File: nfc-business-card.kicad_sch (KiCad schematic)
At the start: 8 parts, among them U1 NT3H2111W0FHKH

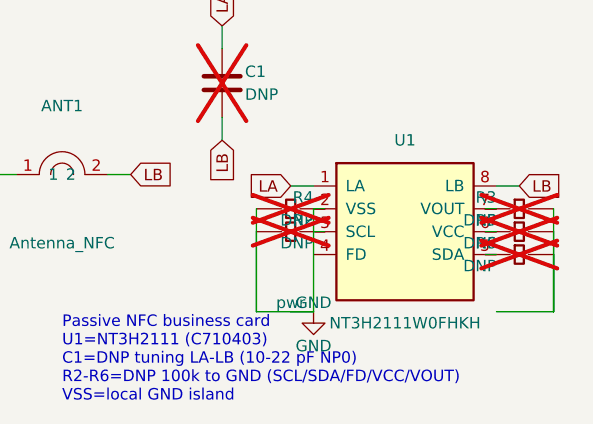
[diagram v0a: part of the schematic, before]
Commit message: fix: route LB under LA skirt without shorting VOUT
Keep the westbound VOUT crossing on F.Cu above the LA skirt, and drop
to B.Cu only in the clearance column between VCC and VOUT. Lower the
KiCad min track width to the JLC floor so intentional 0.15 mm NC stubs
pass DRC.
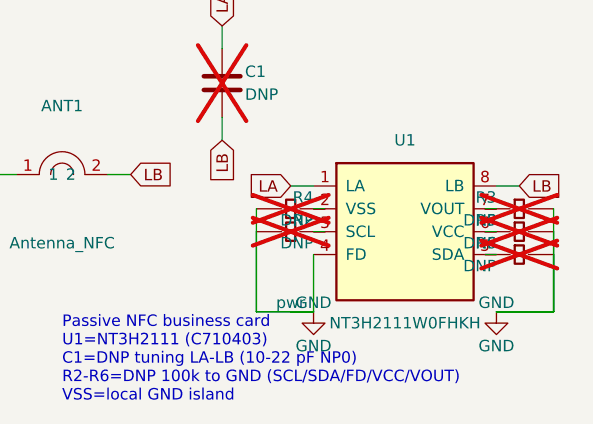
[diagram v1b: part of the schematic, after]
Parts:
- R2, R3, R4, R5, R6: LCSC Part # C25744 -> C60491
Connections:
- net GND: now also R3.1, R5.1, R6.1, U1.4 (FD); no longer R4.2, U1.2 (VSS)
- new net: R4.2, U1.2 (VSS)
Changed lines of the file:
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@@
+	)
+	(symbol
+		(lib_id "NFC_BusinessCard:GND")
+		(at 137.16 93.98 0)
+		(unit 1)
+		(exclude_from_sim no)
+		(in_bom no)
+		(on_board no)
+		(dnp no)
+		(property "Reference" "#PWR02" (at 137.16 100.33 0) (effects (font (size 1.27 1.27)) (hide yes)))
+		(property "Value" "GND" (at 137.16 97.79 0) (effects (font (size 1.27 1.27))))
+		(property "Footprint" "" (at 137.16 93.98 0) (effects (font (size 1.27 1.27)) (hide yes)))
+		(pin "1")
+		(instances (project "nfc-business-card" (path "/db0e1d12-1252-490b-9c29-4e9a9001ab69" (reference "#PWR02") (unit 1))))
 	)
 	(symbol
@@
 	(wire (pts (xy 106.68 64.77) (xy 106.68 62.23)) (stroke (width 0) (type default)))
 	(global_label "LA" (shape input) (at 106.68 62.23 90) (effects (font (size 1.27 1.27)) (justify left bottom)))
-	(wire (pts (xy 116.84 82.55) (xy 116.84 93.98)) (stroke (width 0) (type default)))
+	(wire (pts (xy 116.84 87.63) (xy 116.84 93.98)) (stroke (width 0) (type default)))
 	(wire (pts (xy 116.84 93.98) (xy 114.3 93.98)) (stroke (width 0) (type default)))
 	(symbol
@@
 		(property "Value" "DNP" (at 116.84 86.36 90) (effects (font (size 1.27 1.27)) (justify left)))
 		(property "Footprint" "NFC_BusinessCard:R_0402_1005Metric" (at 114.3 85.09 90) (effects (font (size 1.27 1.27)) (hide yes)))
-		(property "LCSC Part #" "C25744" (at 114.3 85.09 90) (effects (font (size 1.27 1.27)) (hide yes)))
+		(property "LCSC Part #" "C60491" (at 114.3 85.09 90) (effects (font (size 1.27 1.27)) (hide yes)))
 		(pin "1")
 		(pin "2")
@@
 	(wire (pts (xy 116.84 85.09) (xy 118.11 85.09)) (stroke (width 0) (type default)))
 	(wire (pts (xy 110.49 85.09) (xy 110.49 93.98)) (stroke (width 0) (type default)))
+	(wire (pts (xy 110.49 93.98) (xy 116.84 93.98)) (stroke (width 0) (type default)))
 	(symbol
 		(lib_id "NFC_BusinessCard:R_0402")
@@
 		(property "Value" "DNP" (at 116.84 83.82 90) (effects (font (size 1.27 1.27)) (justify left)))
 		(property "Footprint" "NFC_BusinessCard:R_0402_1005Metric" (at 114.3 82.55 90) (effects (font (size 1.27 1.27)) (hide yes)))
-		(property "LCSC Part #" "C25744" (at 114.3 82.55 90) (effects (font (size 1.27 1.27)) (hide yes)))
+		(property "LCSC Part #" "C60491" (at 114.3 82.55 90) (effects (font (size 1.27 1.27)) (hide yes)))
 		(pin "1")
 		(pin "2")
@@
 	(wire (pts (xy 116.84 82.55) (xy 118.11 82.55)) (stroke (width 0) (type default)))
 	(wire (pts (xy 110.49 82.55) (xy 110.49 93.98)) (stroke (width 0) (type default)))
+	(wire (pts (xy 110.49 93.98) (xy 116.84 93.98)) (stroke (width 0) (type default)))
 	(symbol
 		(lib_id "NFC_BusinessCard:R_0402")
@@
 		(property "Value" "DNP" (at 137.16 83.82 270) (effects (font (size 1.27 1.27)) (justify left)))
 		(property "Footprint" "NFC_BusinessCard:R_0402_1005Metric" (at 139.7 82.55 270) (effects (font (size 1.27 1.27)) (hide yes)))
-		(property "LCSC Part #" "C25744" (at 139.7 82.55 270) (effects (font (size 1.27 1.27)) (hide yes)))
+		(property "LCSC Part #" "C60491" (at 139.7 82.55 270) (effects (font (size 1.27 1.27)) (hide yes)))
 		(pin "1")
 		(pin "2")
@@
 	(wire (pts (xy 137.16 82.55) (xy 135.89 82.55)) (stroke (width 0) (type default)))
 	(wire (pts (xy 143.51 82.55) (xy 143.51 93.98)) (stroke (width 0) (type default)))
+	(wire (pts (xy 143.51 93.98) (xy 137.16 93.98)) (stroke (width 0) (type default)))
 	(symbol
 		(lib_id "NFC_BusinessCard:R_0402")
@@
 		(property "Value" "DNP" (at 137.16 86.36 270) (effects (font (size 1.27 1.27)) (justify left)))
 		(property "Footprint" "NFC_BusinessCard:R_0402_1005Metric" (at 139.7 85.09 270) (effects (font (size 1.27 1.27)) (hide yes)))
-		(property "LCSC Part #" "C25744" (at 139.7 85.09 270) (effects (font (size 1.27 1.27)) (hide yes)))
+		(property "LCSC Part #" "C60491" (at 139.7 85.09 270) (effects (font (size 1.27 1.27)) (hide yes)))
 		(pin "1")
 		(pin "2")
@@
 	(wire (pts (xy 137.16 85.09) (xy 135.89 85.09)) (stroke (width 0) (type default)))
 	(wire (pts (xy 143.51 85.09) (xy 143.51 93.98)) (stroke (width 0) (type default)))
+	(wire (pts (xy 143.51 93.98) (xy 137.16 93.98)) (stroke (width 0) (type default)))
 	(symbol
 		(lib_id "NFC_BusinessCard:R_0402")
-		(at 139.7 87.63 270)
+		(at 139.7 87.63000000000001 270)
 		(unit 1)
 		(exclude_from_sim no)
@@
 		(on_board yes)
 		(dnp yes)
-		(property "Reference" "R6" (at 137.16 86.36 270) (effects (font (size 1.27 1.27)) (justify left)))
-		(property "Value" "DNP" (at 137.16 88.89999999999999 270) (effects (font (size 1.27 1.27)) (justify left)))
-		(property "Footprint" "NFC_BusinessCard:R_0402_1005Metric" (at 139.7 87.63 270) (effects (font (size 1.27 1.27)) (hide yes)))
-		(property "LCSC Part #" "C25744" (at 139.7 87.63 270) (effects (font (size 1.27 1.27)) (hide yes)))
+		(property "Reference" "R6" (at 137.16 86.36000000000001 270) (effects (font (size 1.27 1.27)) (justify left)))
+		(property "Value" "DNP" (at 137.16 88.9 270) (effects (font (size 1.27 1.27)) (justify left)))
+		(property "Footprint" "NFC_BusinessCard:R_0402_1005Metric" (at 139.7 87.63000000000001 270) (effects (font (size 1.27 1.27)) (hide yes)))
+		(property "LCSC Part #" "C60491" (at 139.7 87.63000000000001 270) (effects (font (size 1.27 1.27)) (hide yes)))
 		(pin "1")
 		(pin "2")
 		(instances (project "nfc-business-card" (path "/db0e1d12-1252-490b-9c29-4e9a9001ab69" (reference "R6") (unit 1))))
 	)
-	(wire (pts (xy 137.16 87.63) (xy 135.89 87.63)) (stroke (width 0) (type default)))
-	(wire (pts (xy 143.51 87.63) (xy 143.51 93.98)) (stroke (width 0) (type default)))
-	(wire (pts (xy 110.49 93.98) (xy 116.84 93.98)) (stroke (width 0) (type default)))
-	(wire (pts (xy 116.84 93.98) (xy 116.84 93.98)) (stroke (width 0) (type default)))
+	(wire (pts (xy 137.16 87.63000000000001) (xy 135.89 87.63000000000001)) (stroke (width 0) (type default)))
+	(wire (pts (xy 143.51 87.63000000000001) (xy 143.51 93.98)) (stroke (width 0) (type default)))
 	(wire (pts (xy 143.51 93.98) (xy 137.16 93.98)) (stroke (width 0) (type default)))
-	(wire (pts (xy 137.16 93.98) (xy 137.16 93.98)) (stroke (width 0) (type default)))
 	(text "Passive NFC business card\nU1=NT3H2111 (C710403)\nC1=DNP tuning LA-LB (10-22 pF NP0)\nR2-R6=DNP 100k to GND (SCL/SDA/FD/VCC/VOUT)\nVSS=local GND island"
 		(at 88.9 104.14 0)

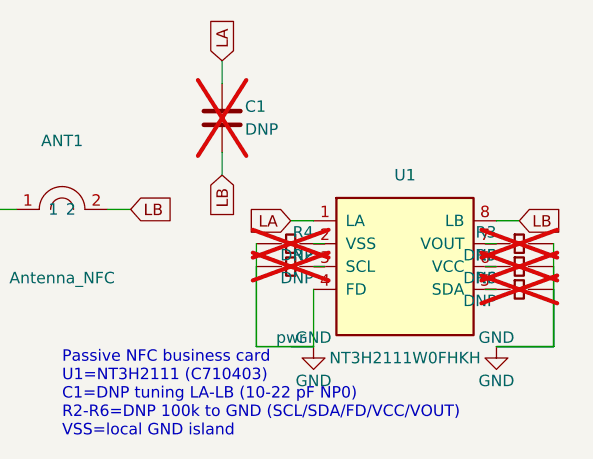
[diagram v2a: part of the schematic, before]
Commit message: fix: clear schematic parity and stop greenwashing DRC warnings
Correct eeschema Y mapping for U1–R NC wiring, skip degenerate VOUT
segments, require CLI checks to fail on unaccepted warnings/parity, and
only allowlist LA/LB for clearance (not crossings).
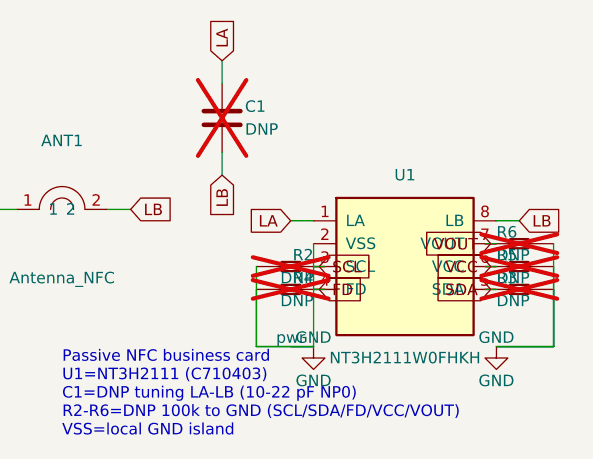
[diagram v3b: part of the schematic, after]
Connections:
- net GND: now also R2.2, R3.2, R4.2, R5.2, R6.2, U1.2 (VSS); no longer R2.1, R3.1, R4.1, R5.1, R6.1, U1.4 (FD)
- net VCC: now reaches U1.6 (VCC)
- net VCC: now also R5.1; no longer R5.2
- net VOUT: now reaches U1.7 (VOUT)
- net VOUT: now also R6.1; no longer R3.2
- net SDA: now reaches U1.5 (SDA)
- net SDA: now also R3.1; no longer R6.2
- net SCL: now reaches U1.3 (SCL)
- net SCL: now also R2.1; no longer R2.2
- new net FD: R4.1, U1.4 (FD)
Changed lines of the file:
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@@
 	(wire (pts (xy 106.68 64.77) (xy 106.68 62.23)) (stroke (width 0) (type default)))
 	(global_label "LA" (shape input) (at 106.68 62.23 90) (effects (font (size 1.27 1.27)) (justify left bottom)))
-	(wire (pts (xy 116.84 87.63) (xy 116.84 93.98)) (stroke (width 0) (type default)))
+	(wire (pts (xy 116.84 82.55) (xy 116.84 93.98)) (stroke (width 0) (type default)))
 	(wire (pts (xy 116.84 93.98) (xy 114.3 93.98)) (stroke (width 0) (type default)))
 	(symbol
 		(lib_id "NFC_BusinessCard:R_0402")
-		(at 114.3 85.09 90)
+		(at 114.3 85.09 180)
 		(unit 1)
 		(exclude_from_sim no)
@@
 		(on_board yes)
 		(dnp yes)
-		(property "Reference" "R2" (at 116.84 83.82000000000001 90) (effects (font (size 1.27 1.27)) (justify left)))
-		(property "Value" "DNP" (at 116.84 86.36 90) (effects (font (size 1.27 1.27)) (justify left)))
-		(property "Footprint" "NFC_BusinessCard:R_0402_1005Metric" (at 114.3 85.09 90) (effects (font (size 1.27 1.27)) (hide yes)))
-		(property "LCSC Part #" "C60491" (at 114.3 85.09 90) (effects (font (size 1.27 1.27)) (hide yes)))
+		(property "Reference" "R2" (at 116.84 83.82000000000001 0) (effects (font (size 1.27 1.27)) (justify left)))
+		(property "Value" "DNP" (at 116.84 86.36 0) (effects (font (size 1.27 1.27)) (justify left)))
+		(property "Footprint" "NFC_BusinessCard:R_0402_1005Metric" (at 114.3 85.09 180) (effects (font (size 1.27 1.27)) (hide yes)))
+		(property "Description" "100k NC pull-down" (at 114.3 85.09 180) (effects (font (size 1.27 1.27)) (hide yes)))
+		(property "LCSC Part #" "C60491" (at 114.3 85.09 180) (effects (font (size 1.27 1.27)) (hide yes)))
 		(pin "1")
 		(pin "2")
@@
 	)
 	(wire (pts (xy 116.84 85.09) (xy 118.11 85.09)) (stroke (width 0) (type default)))
+	(global_label "SCL" (shape input) (at 117.475 85.09 0) (effects (font (size 1.27 1.27)) (justify left bottom)))
 	(wire (pts (xy 110.49 85.09) (xy 110.49 93.98)) (stroke (width 0) (type default)))
 	(wire (pts (xy 110.49 93.98) (xy 116.84 93.98)) (stroke (width 0) (type default)))
 	(symbol
 		(lib_id "NFC_BusinessCard:R_0402")
-		(at 114.3 82.55 90)
+		(at 114.3 87.63000000000001 180)
 		(unit 1)
 		(exclude_from_sim no)
@@
 		(on_board yes)
 		(dnp yes)
-		(property "Reference" "R4" (at 116.84 81.28 90) (effects (font (size 1.27 1.27)) (justify left)))
-		(property "Value" "DNP" (at 116.84 83.82 90) (effects (font (size 1.27 1.27)) (justify left)))
-		(property "Footprint" "NFC_BusinessCard:R_0402_1005Metric" (at 114.3 82.55 90) (effects (font (size 1.27 1.27)) (hide yes)))
-		(property "LCSC Part #" "C60491" (at 114.3 82.55 90) (effects (font (size 1.27 1.27)) (hide yes)))
+		(property "Reference" "R4" (at 116.84 86.36000000000001 0) (effects (font (size 1.27 1.27)) (justify left)))
+		(property "Value" "DNP" (at 116.84 88.9 0) (effects (font (size 1.27 1.27)) (justify left)))
+		(property "Footprint" "NFC_BusinessCard:R_0402_1005Metric" (at 114.3 87.63000000000001 180) (effects (font (size 1.27 1.27)) (hide yes)))
+		(property "Description" "100k NC pull-down" (at 114.3 87.63000000000001 180) (effects (font (size 1.27 1.27)) (hide yes)))
+		(property "LCSC Part #" "C60491" (at 114.3 87.63000000000001 180) (effects (font (size 1.27 1.27)) (hide yes)))
 		(pin "1")
 		(pin "2")
 		(instances (project "nfc-business-card" (path "/db0e1d12-1252-490b-9c29-4e9a9001ab69" (reference "R4") (unit 1))))
 	)
-	(wire (pts (xy 116.84 82.55) (xy 118.11 82.55)) (stroke (width 0) (type default)))
-	(wire (pts (xy 110.49 82.55) (xy 110.49 93.98)) (stroke (width 0) (type default)))
+	(wire (pts (xy 116.84 87.63000000000001) (xy 118.11 87.63000000000001)) (stroke (width 0) (type default)))
+	(global_label "FD" (shape input) (at 117.475 87.63000000000001 0) (effects (font (size 1.27 1.27)) (justify left bottom)))
+	(wire (pts (xy 110.49 87.63000000000001) (xy 110.49 93.98)) (stroke (width 0) (type default)))
 	(wire (pts (xy 110.49 93.98) (xy 116.84 93.98)) (stroke (width 0) (type default)))
 	(symbol
 		(lib_id "NFC_BusinessCard:R_0402")
-		(at 139.7 82.55 270)
+		(at 139.7 87.63000000000001 0)
 		(unit 1)
 		(exclude_from_sim no)
@@
 		(on_board yes)
 		(dnp yes)
-		(property "Reference" "R3" (at 137.16 81.28 270) (effects (font (size 1.27 1.27)) (justify left)))
-		(property "Value" "DNP" (at 137.16 83.82 270) (effects (font (size 1.27 1.27)) (justify left)))
-		(property "Footprint" "NFC_BusinessCard:R_0402_1005Metric" (at 139.7 82.55 270) (effects (font (size 1.27 1.27)) (hide yes)))
-		(property "LCSC Part #" "C60491" (at 139.7 82.55 270) (effects (font (size 1.27 1.27)) (hide yes)))
+		(property "Reference" "R3" (at 137.16 86.36000000000001 0) (effects (font (size 1.27 1.27)) (justify left)))
+		(property "Value" "DNP" (at 137.16 88.9 0) (effects (font (size 1.27 1.27)) (justify left)))
+		(property "Footprint" "NFC_BusinessCard:R_0402_1005Metric" (at 139.7 87.63000000000001 0) (effects (font (size 1.27 1.27)) (hide yes)))
+		(property "Description" "100k NC pull-down" (at 139.7 87.63000000000001 0) (effects (font (size 1.27 1.27)) (hide yes)))
+		(property "LCSC Part #" "C60491" (at 139.7 87.63000000000001 0) (effects (font (size 1.27 1.27)) (hide yes)))
 		(pin "1")
 		(pin "2")
 		(instances (project "nfc-business-card" (path "/db0e1d12-1252-490b-9c29-4e9a9001ab69" (reference "R3") (unit 1))))
 	)
-	(wire (pts (xy 137.16 82.55) (xy 135.89 82.55)) (stroke (width 0) (type default)))
-	(wire (pts (xy 143.51 82.55) (xy 143.51 93.98)) (stroke (width 0) (type default)))
+	(wire (pts (xy 137.16 87.63000000000001) (xy 135.89 87.63000000000001)) (stroke (width 0) (type default)))
+	(global_label "SDA" (shape input) (at 136.52499999999998 87.63000000000001 180) (effects (font (size 1.27 1.27)) (justify right bottom)))
+	(wire (pts (xy 143.51 87.63000000000001) (xy 143.51 93.98)) (stroke (width 0) (type default)))
 	(wire (pts (xy 143.51 93.98) (xy 137.16 93.98)) (stroke (width 0) (type default)))
 	(symbol
 		(lib_id "NFC_BusinessCard:R_0402")
-		(at 139.7 85.09 270)
+		(at 139.7 85.09 0)
 		(unit 1)
 		(exclude_from_sim no)
@@
 		(on_board yes)
 		(dnp yes)
-		(property "Reference" "R5" (at 137.16 83.82000000000001 270) (effects (font (size 1.27 1.27)) (justify left)))
-		(property "Value" "DNP" (at 137.16 86.36 270) (effects (font (size 1.27 1.27)) (justify left)))
-		(property "Footprint" "NFC_BusinessCard:R_0402_1005Metric" (at 139.7 85.09 270) (effects (font (size 1.27 1.27)) (hide yes)))
-		(property "LCSC Part #" "C60491" (at 139.7 85.09 270) (effects (font (size 1.27 1.27)) (hide yes)))
+		(property "Reference" "R5" (at 137.16 83.82000000000001 0) (effects (font (size 1.27 1.27)) (justify left)))
+		(property "Value" "DNP" (at 137.16 86.36 0) (effects (font (size 1.27 1.27)) (justify left)))
+		(property "Footprint" "NFC_BusinessCard:R_0402_1005Metric" (at 139.7 85.09 0) (effects (font (size 1.27 1.27)) (hide yes)))
+		(property "Description" "100k NC pull-down" (at 139.7 85.09 0) (effects (font (size 1.27 1.27)) (hide yes)))
+		(property "LCSC Part #" "C60491" (at 139.7 85.09 0) (effects (font (size 1.27 1.27)) (hide yes)))
 		(pin "1")
 		(pin "2")
@@
 	)
 	(wire (pts (xy 137.16 85.09) (xy 135.89 85.09)) (stroke (width 0) (type default)))
+	(global_label "VCC" (shape input) (at 136.52499999999998 85.09 180) (effects (font (size 1.27 1.27)) (justify right bottom)))
 	(wire (pts (xy 143.51 85.09) (xy 143.51 93.98)) (stroke (width 0) (type default)))
 	(wire (pts (xy 143.51 93.98) (xy 137.16 93.98)) (stroke (width 0) (type default)))
 	(symbol
 		(lib_id "NFC_BusinessCard:R_0402")
-		(at 139.7 87.63000000000001 270)
+		(at 139.7 82.55 0)
 		(unit 1)
 		(exclude_from_sim no)
@@
 		(on_board yes)
 		(dnp yes)
-		(property "Reference" "R6" (at 137.16 86.36000000000001 270) (effects (font (size 1.27 1.27)) (justify left)))
-		(property "Value" "DNP" (at 137.16 88.9 270) (effects (font (size 1.27 1.27)) (justify left)))
-		(property "Footprint" "NFC_BusinessCard:R_0402_1005Metric" (at 139.7 87.63000000000001 270) (effects (font (size 1.27 1.27)) (hide yes)))
-		(property "LCSC Part #" "C60491" (at 139.7 87.63000000000001 270) (effects (font (size 1.27 1.27)) (hide yes)))
+		(property "Reference" "R6" (at 137.16 81.28 0) (effects (font (size 1.27 1.27)) (justify left)))
+		(property "Value" "DNP" (at 137.16 83.82 0) (effects (font (size 1.27 1.27)) (justify left)))
+		(property "Footprint" "NFC_BusinessCard:R_0402_1005Metric" (at 139.7 82.55 0) (effects (font (size 1.27 1.27)) (hide yes)))
+		(property "Description" "100k NC pull-down" (at 139.7 82.55 0) (effects (font (size 1.27 1.27)) (hide yes)))
+		(property "LCSC Part #" "C60491" (at 139.7 82.55 0) (effects (font (size 1.27 1.27)) (hide yes)))
 		(pin "1")
 		(pin "2")
 		(instances (project "nfc-business-card" (path "/db0e1d12-1252-490b-9c29-4e9a9001ab69" (reference "R6") (unit 1))))
 	)
-	(wire (pts (xy 137.16 87.63000000000001) (xy 135.89 87.63000000000001)) (stroke (width 0) (type default)))
-	(wire (pts (xy 143.51 87.63000000000001) (xy 143.51 93.98)) (stroke (width 0) (type default)))
+	(wire (pts (xy 137.16 82.55) (xy 135.89 82.55)) (stroke (width 0) (type default)))
+	(global_label "VOUT" (shape input) (at 136.52499999999998 82.55 180) (effects (font (size 1.27 1.27)) (justify right bottom)))
+	(wire (pts (xy 143.51 82.55) (xy 143.51 93.98)) (stroke (width 0) (type default)))
 	(wire (pts (xy 143.51 93.98) (xy 137.16 93.98)) (stroke (width 0) (type default)))
 	(text "Passive NFC business card\nU1=NT3H2111 (C710403)\nC1=DNP tuning LA-LB (10-22 pF NP0)\nR2-R6=DNP 100k to GND (SCL/SDA/FD/VCC/VOUT)\nVSS=local GND island"
